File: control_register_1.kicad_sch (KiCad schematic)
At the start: 7 parts, among them U10 74HC375, U11 74HC02, U12 74HC21, U13 74HC21, U15 74AHC1G08, U7 74HC04, U9 74HC375

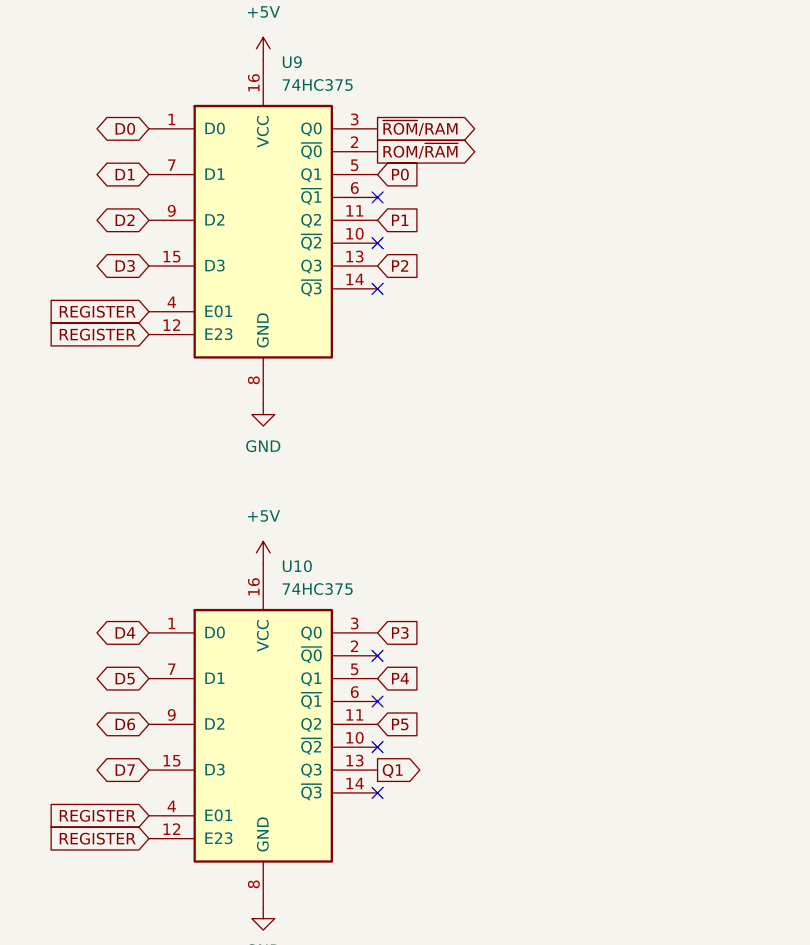
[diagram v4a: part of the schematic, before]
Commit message: move paged memory to external board
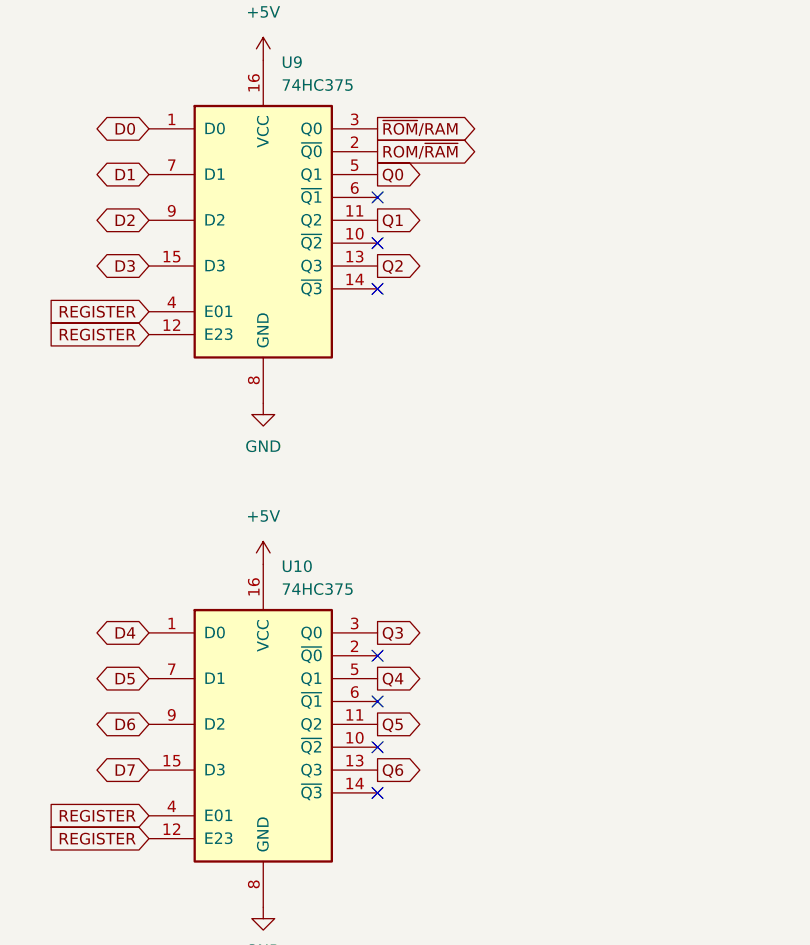
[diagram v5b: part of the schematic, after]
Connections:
- net P1 is gone; now on net Q1: U9.11 (Q2)
- net Q1: no longer U10.13 (Q3)
- net P0 renamed Q0
- net P2 renamed Q2
- net P3 renamed Q3
- net P4 renamed Q4
- net P5 renamed Q5
- new net Q6: U10.13 (Q3)
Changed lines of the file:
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@@
     (stroke (width 0) (type default) (color 0 0 0 0))
   )
+  (global_label "Q2" (shape output) (at 164.084 52.959 0) (fields_autoplaced)
+    (effects (font (size 1.27 1.27)) (justify left))
+    (property "Intersheet References" "${INTERSHEET_REFS}" (id 0) (at 169.0371 52.8796 0)
+      (effects (font (size 1.27 1.27)) (justify left) hide)
+    )
+  )
   (global_label "R{slash}~{W}" (shape input) (at 77.978 40.894 90) (fields_autoplaced)
     (effects (font (size 1.27 1.27)) (justify left))
@@
     )
   )
+  (global_label "Q0" (shape output) (at 164.084 42.799 0) (fields_autoplaced)
+    (effects (font (size 1.27 1.27)) (justify left))
+    (property "Intersheet References" "${INTERSHEET_REFS}" (id 0) (at 169.0371 42.7196 0)
+      (effects (font (size 1.27 1.27)) (justify left) hide)
+    )
+  )
   (global_label "A2" (shape input) (at 47.752 83.439 180) (fields_autoplaced)
     (effects (font (size 1.27 1.27)) (justify right))
@@
     )
   )
+  (global_label "Q1" (shape output) (at 164.084 47.879 0) (fields_autoplaced)
+    (effects (font (size 1.27 1.27)) (justify left))
+    (property "Intersheet References" "${INTERSHEET_REFS}" (id 0) (at 169.0371 47.9584 0)
+      (effects (font (size 1.27 1.27)) (justify left) hide)
+    )
+  )
   (global_label "D6" (shape bidirectional) (at 138.684 103.886 180) (fields_autoplaced)
     (effects (font (size 1.27 1.27)) (justify right))
@@
     )
   )
-  (global_label "P0" (shape input) (at 164.084 42.799 0) (fields_autoplaced)
-    (effects (font (size 1.27 1.27)) (justify left))
-    (property "Intersheet References" "${INTERSHEET_REFS}" (id 0) (at 168.9766 42.7196 0)
+  (global_label "Q5" (shape output) (at 164.084 103.886 0) (fields_autoplaced)
+    (effects (font (size 1.27 1.27)) (justify left))
+    (property "Intersheet References" "${INTERSHEET_REFS}" (id 0) (at 169.0371 103.8066 0)
       (effects (font (size 1.27 1.27)) (justify left) hide)
     )
@@
     )
   )
-  (global_label "Q1" (shape output) (at 164.084 108.966 0) (fields_autoplaced)
-    (effects (font (size 1.27 1.27)) (justify left))
-    (property "Intersheet References" "${INTERSHEET_REFS}" (id 0) (at 169.0371 109.0454 0)
-      (effects (font (size 1.27 1.27)) (justify left) hide)
-    )
-  )
   (global_label "A6" (shape input) (at 45.72 69.342 180) (fields_autoplaced)
     (effects (font (size 1.27 1.27)) (justify right))
@@
     )
   )
+  (global_label "Q6" (shape output) (at 164.084 108.966 0) (fields_autoplaced)
+    (effects (font (size 1.27 1.27)) (justify left))
+    (property "Intersheet References" "${INTERSHEET_REFS}" (id 0) (at 169.0371 108.8866 0)
+      (effects (font (size 1.27 1.27)) (justify left) hide)
+    )
+  )
   (global_label "REGISTER" (shape input) (at 138.684 58.039 180) (fields_autoplaced)
     (effects (font (size 1.27 1.27)) (justify right))
@@
     )
   )
-  (global_label "P3" (shape input) (at 164.084 93.726 0) (fields_autoplaced)
-    (effects (font (size 1.27 1.27)) (justify left))
-    (property "Intersheet References" "${INTERSHEET_REFS}" (id 0) (at 168.9766 93.6466 0)
-      (effects (font (size 1.27 1.27)) (justify left) hide)
-    )
-  )
   (global_label "A14" (shape input) (at 45.72 44.958 180) (fields_autoplaced)
     (effects (font (size 1.27 1.27)) (justify right))
@@
     )
   )
+  (global_label "Q4" (shape output) (at 164.084 98.806 0) (fields_autoplaced)
+    (effects (font (size 1.27 1.27)) (justify left))
+    (property "Intersheet References" "${INTERSHEET_REFS}" (id 0) (at 169.0371 98.7266 0)
+      (effects (font (size 1.27 1.27)) (justify left) hide)
+    )
+  )
   (global_label "REGISTER" (shape input) (at 138.684 116.586 180) (fields_autoplaced)
     (effects (font (size 1.27 1.27)) (justify right))
@@
     )
   )
-  (global_label "P4" (shape input) (at 164.084 98.806 0) (fields_autoplaced)
-    (effects (font (size 1.27 1.27)) (justify left))
-    (property "Intersheet References" "${INTERSHEET_REFS}" (id 0) (at 168.9766 98.7266 0)
-      (effects (font (size 1.27 1.27)) (justify left) hide)
-    )
-  )
   (global_label "D2" (shape bidirectional) (at 138.684 47.879 180) (fields_autoplaced)
     (effects (font (size 1.27 1.27)) (justify right))
@@
     )
   )
-  (global_label "P1" (shape input) (at 164.084 47.879 0) (fields_autoplaced)
-    (effects (font (size 1.27 1.27)) (justify left))
-    (property "Intersheet References" "${INTERSHEET_REFS}" (id 0) (at 168.9766 47.7996 0)
-      (effects (font (size 1.27 1.27)) (justify left) hide)
-    )
-  )
   (global_label "A15" (shape input) (at 45.72 47.498 180) (fields_autoplaced)
     (effects (font (size 1.27 1.27)) (justify right))
@@
     )
   )
-  (global_label "P2" (shape input) (at 164.084 52.959 0) (fields_autoplaced)
-    (effects (font (size 1.27 1.27)) (justify left))
-    (property "Intersheet References" "${INTERSHEET_REFS}" (id 0) (at 168.9766 52.8796 0)
-      (effects (font (size 1.27 1.27)) (justify left) hide)
-    )
-  )
   (global_label "D0" (shape bidirectional) (at 138.684 37.719 180) (fields_autoplaced)
     (effects (font (size 1.27 1.27)) (justify right))
@@
     )
   )
-  (global_label "P5" (shape input) (at 164.084 103.886 0) (fields_autoplaced)
-    (effects (font (size 1.27 1.27)) (justify left))
-    (property "Intersheet References" "${INTERSHEET_REFS}" (id 0) (at 168.9766 103.8066 0)
-      (effects (font (size 1.27 1.27)) (justify left) hide)
-    )
-  )
   (global_label "REGISTER" (shape input) (at 138.684 114.046 180) (fields_autoplaced)
     (effects (font (size 1.27 1.27)) (justify right))
@@
     )
   )
+  (global_label "Q3" (shape output) (at 164.084 93.726 0) (fields_autoplaced)
+    (effects (font (size 1.27 1.27)) (justify left))
+    (property "Intersheet References" "${INTERSHEET_REFS}" (id 0) (at 169.0371 93.6466 0)
+      (effects (font (size 1.27 1.27)) (justify left) hide)
+    )
+  )

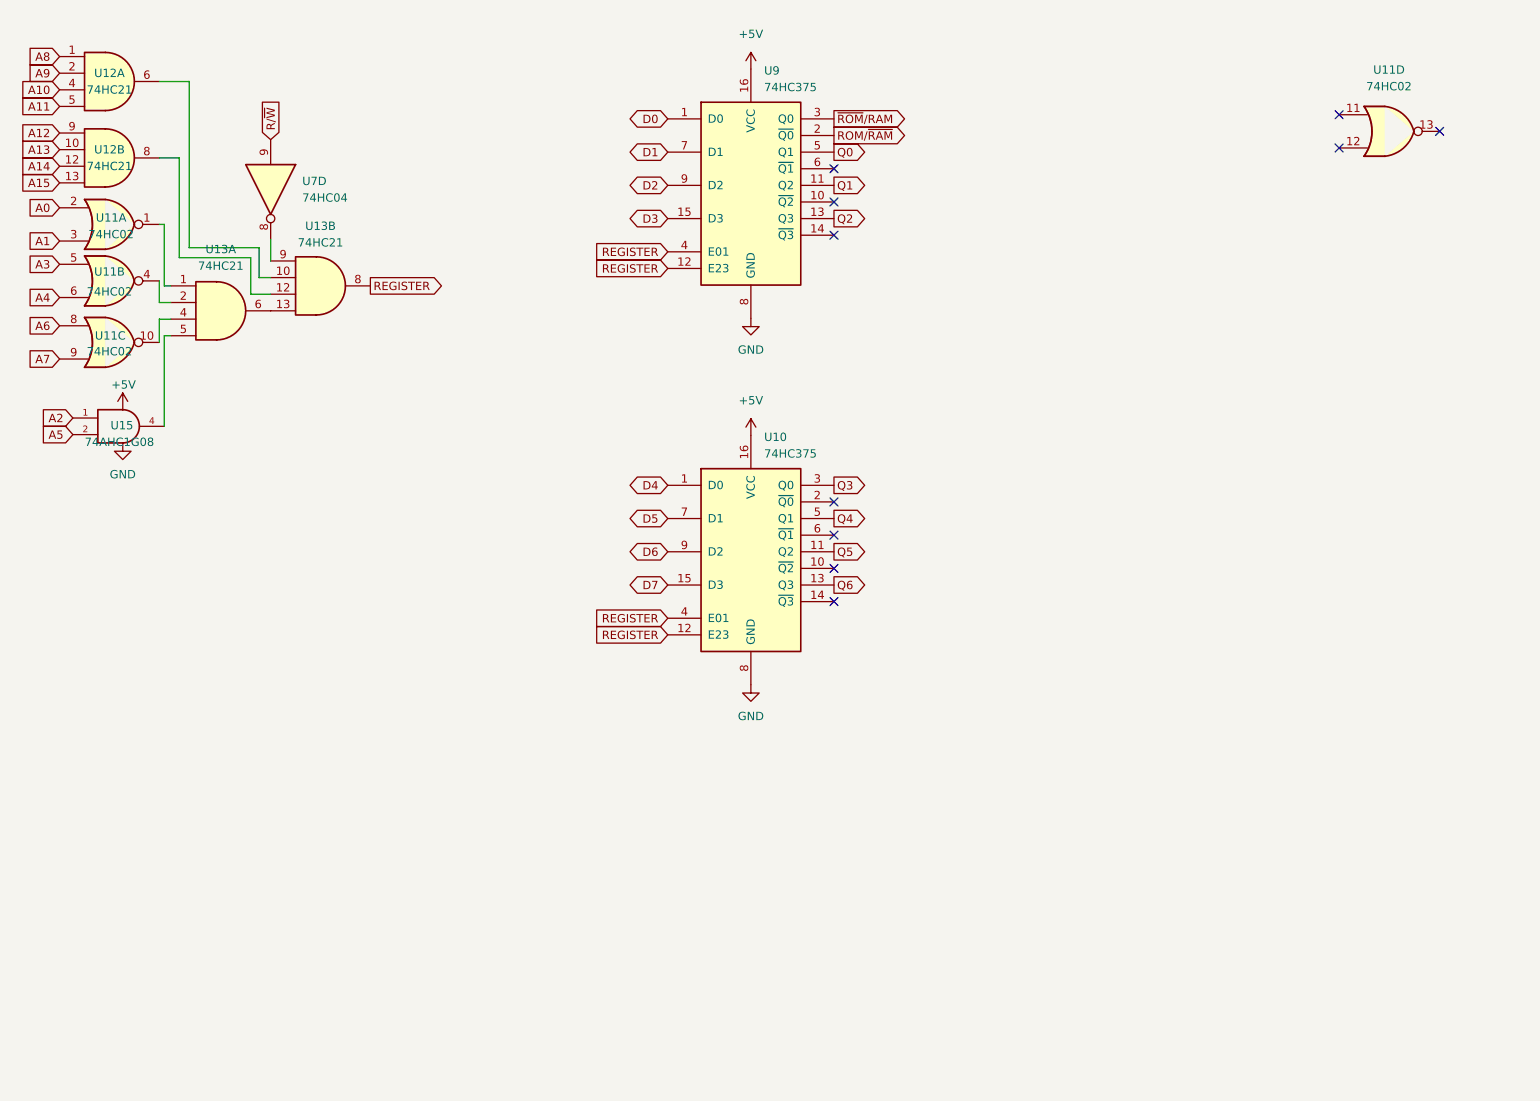
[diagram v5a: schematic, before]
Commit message: modify address logic for mapped registers
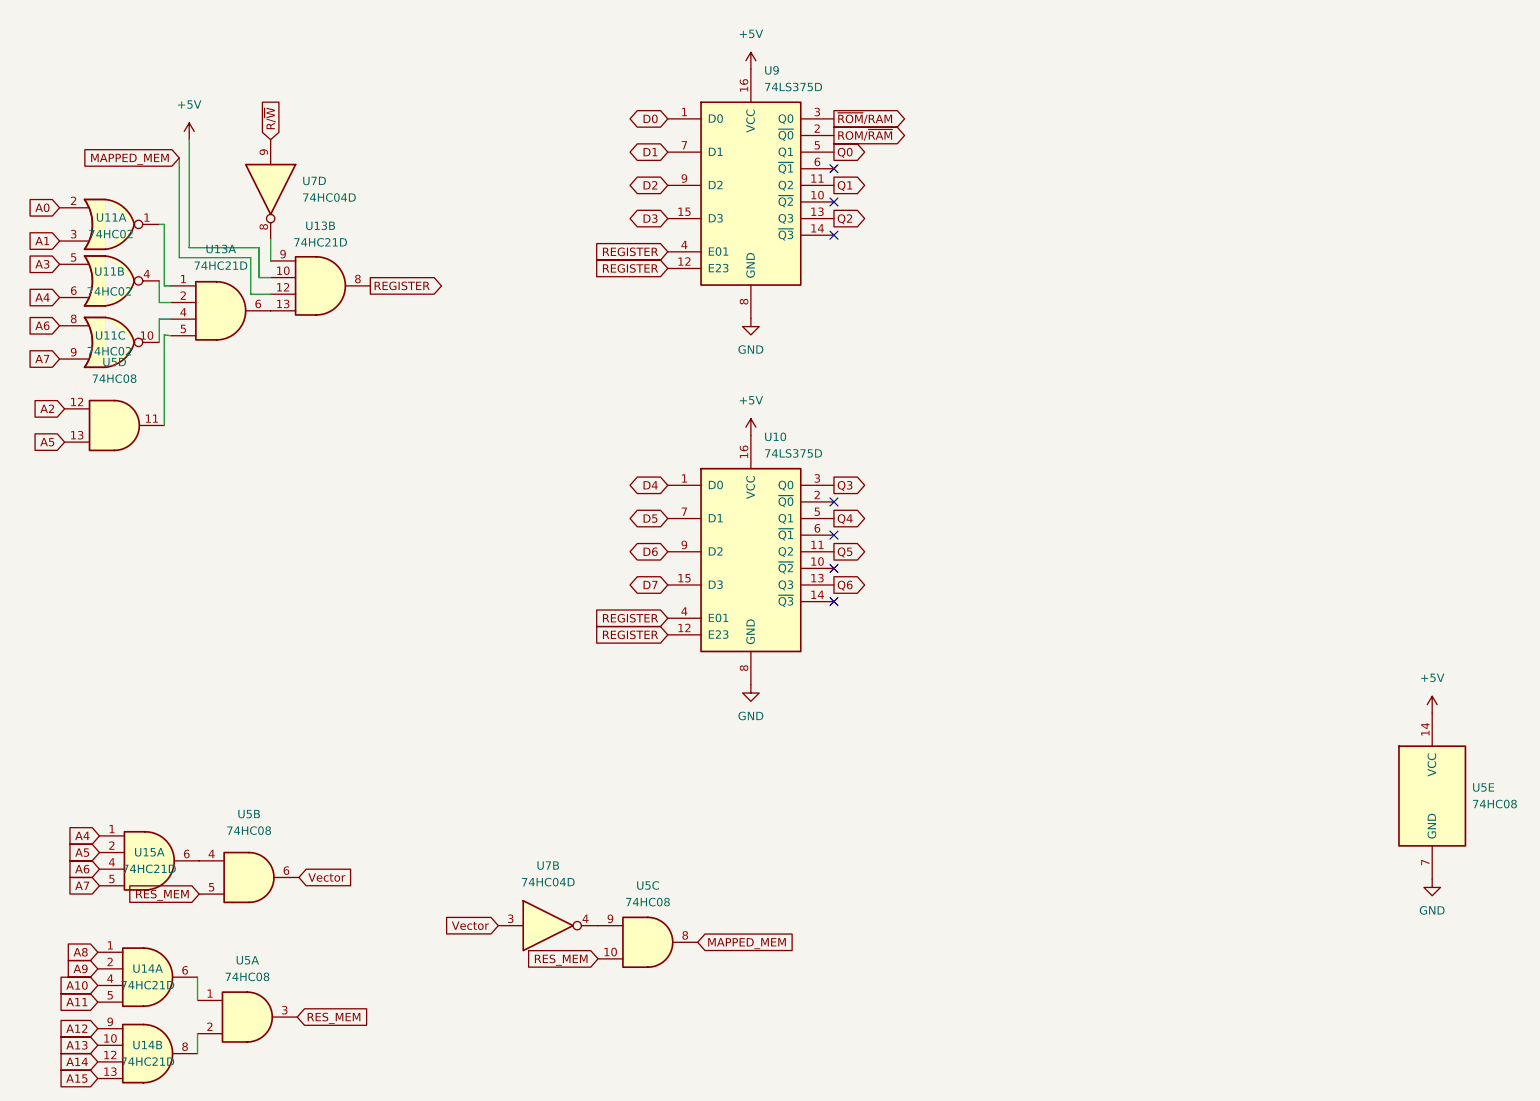
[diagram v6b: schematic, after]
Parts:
- removed unit 4 of U11
- removed U12: 74HC21, Package_SO:SO-14_3.9x8.65mm_P1.27mm, symbol 74xx:74LS21
- removed U15: 74AHC1G08, Package_SO:TSOP-5_1.65x3.05mm_P0.95mm, symbol 74xGxx:74AHC1G08
- added U14, U15: 74HC21D, Package_SO:SOIC-14_3.9x8.7mm_P1.27mm, symbol 74xx:74LS21
- added U5: 74HC08, Package_SO:SOIC-14_3.9x8.7mm_P1.27mm, symbol 74xx:74LS08
- added unit 2 of U7
- U10, U9: value 74HC375 -> 74LS375D
- U13: value 74HC21 -> 74HC21D; footprint Package_SO:SO-14_3.9x8.65mm_P1.27mm -> Package_SO:SOIC-14_3.9x8.7mm_P1.27mm; DigiKey (none) -> 296-8265-5-ND
- U7: value 74HC04 -> 74HC04D; footprint Package_SO:SO-14_3.9x8.65mm_P1.27mm -> Package_SO:SOIC-14_3.9x8.7mm_P1.27mm; DigiKey (none) -> 74HC04DCT-ND
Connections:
- net +5V: now also U13.10, U5.14 (VCC)
- net A10: now also U14.4
- net A11: now also U14.5
- net A12: now also U14.9
- net A13: now also U14.10
- net A14: now also U14.12
- net A15: now also U14.13
- net A2: now also U5.12
- net A4: now also U15.1
- net A5: now also U15.2, U5.13
- net A6: now also U15.4
- net A7: now also U15.5
- net A8: now also U14.1
- net A9: now also U14.2
- net GND: now also U5.7 (GND)
- net at U13.5: now also U5.11
- net MAPPED_MEM: now reaches U13.12
- net MAPPED_MEM: now also U5.8
- new net: U14.6, U5.1
- new net: U14.8, U5.2
- new net: U15.6, U5.4
- new net: U5.9, U7.4
- new net RES_MEM: U5.10, U5.3, U5.5
- new net Vector: U5.6, U7.3
- no-connect marks 10 -> 7
